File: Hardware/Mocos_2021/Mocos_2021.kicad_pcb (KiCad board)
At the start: 2 copper layers, 124.5 x 86.1 mm, 90 parts, among them J1 USB_B_Mini, J2 SERIAL PORT, J3 Programming, Q1 IRFZ44ESTRLPBF, Q2 IRFZ44ESTRLPBF, Q3 IRFZ44ESTRLPBF, Q4 IRFZ44ESTRLPBF, Q5 IRFZ44ESTRLPBF, Q6 IRFZ44ESTRLPBF, U1 DRV8302, U2 STM32F40X_LQFP64, U3 3.3V OKI, X1 8MHz, 10ppm

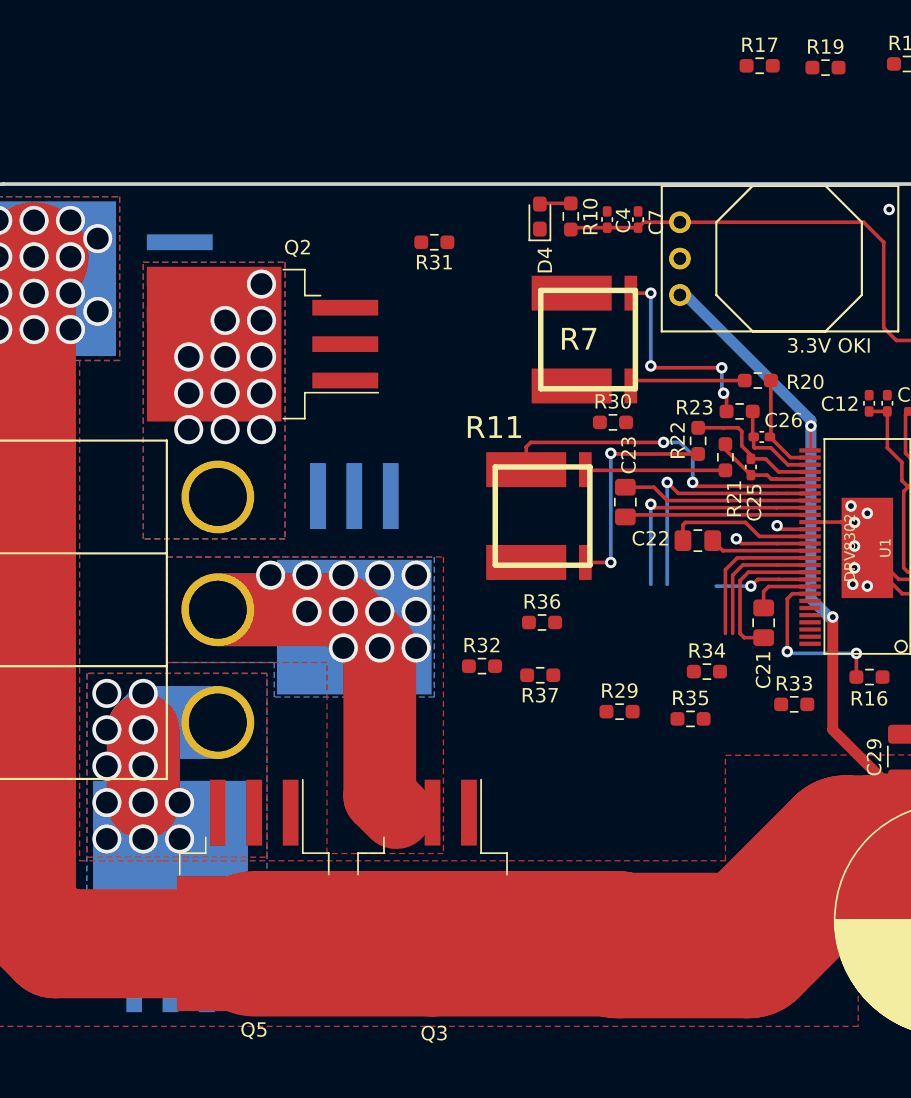
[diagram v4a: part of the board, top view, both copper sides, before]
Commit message: Finished routing all but the sense resistors
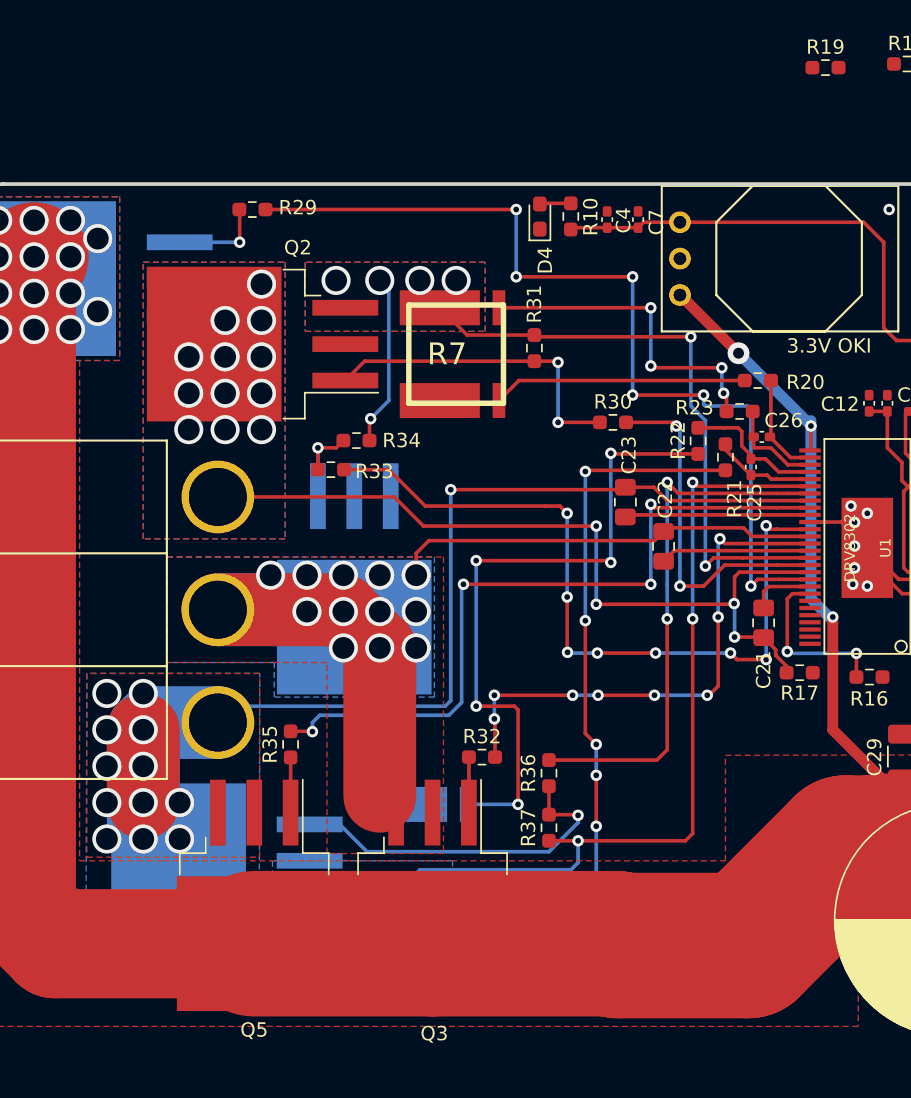
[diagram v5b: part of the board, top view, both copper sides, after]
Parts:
- R11: moved to B.Cu
- moved R29 43.4 mm to (85.1, 71.0)
- moved R17 42.5 mm to (123.3, 103.3), turned to 180 degrees
- moved R33 36.3 mm to (90.6, 89.2)
- moved R34 29.3 mm to (92.4, 87.1), turned to 180 degrees
- moved R35 28.0 mm to (87.8, 108.3), turned to 90 degrees
- moved R11 24.8 mm to (98.9, 115.8), turned to 90 degrees
- moved R37 10.7 mm to (105.8, 114.1), turned to 90 degrees
- moved R36 10.5 mm to (105.8, 110.3), turned to 90 degrees
- moved R31 10.2 mm to (104.8, 80.7), turned to 270 degrees
- moved R7 9.26 mm to (101.2, 81.1)
- moved R32 6.35 mm to (101.1, 109.2)
- moved Q6 4.66 mm to (83.3, 116.5), turned to 180 degrees
- moved C22 2.43 mm to (113.8, 94.5), turned to 270 degrees
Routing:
- net M_H1: track 6.74 -> 64.3 mm, vias 1 -> 6
- net M_L2: track 2.57 -> 53.1 mm, vias 1 -> 8
- net H1_VS: track 10.6 -> 56.9 mm, vias 12 -> 16
- net H3_VS: track 32.4 -> 76.3 mm, vias 12 -> 13
- net H1_LOW: track 10.7 -> 54.3 mm, vias 0 -> 7
- net Net-(R11-Pad3): track 9.80 -> 48.6 mm, vias 0 -> 5
- net M_H3: track 16.8 -> 51.4 mm, vias 1 -> 4
- net H3_LOW: track 23.9 -> 58.1 mm, vias 2 -> 3
- net M_H2: track 5.28 -> 37.0 mm, vias 1 -> 8
- net Net-(R11-Pad4): track 15.5 -> 46.7 mm, vias 2 -> 5
- net Net-(Q6-Pad2): track 0.00 -> 24.9 mm, vias 0 -> 1
- net Net-(Q2-Pad2): track 0.00 -> 22.6 mm, vias 0 -> 2
- net M_L3: track 17.4 -> 37.5 mm, vias 1 -> 2
- net H2_VS: track 46.2 -> 64.1 mm
- net M_L1: track 9.76 -> 24.6 mm, vias 0 -> 2
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- added copper zone on B.Cu, net H1_LOW
- added copper zone on F.Cu, net H1_LOW
- added copper zone on B.Cu, net H3_LOW

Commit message: Finished layout and generated Gerbs
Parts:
- added G***: LOGO, Anthony's Silkscreens:W, B.Cu at (162.4, 149.2)
- added G***: LOGO, MRDT_Silkscreens:z_sig_Anthony_Robles_15mmx8.2mm, F.Cu at (162.3, 149.4)
- U1: value DRV8302 -> DRV8302DCA
- U2: value STM32F40X_LQFP64 -> STM32F405RGT6
- moved R18 46.1 mm to (119.8, 105.6), turned to 90 degrees
- moved R19 20.3 mm to (127.7, 81.2), turned to 180 degrees
- moved C38 5.04 mm to (173.8, 95.8)
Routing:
- net SENSE2: track 9.45 -> 66.9 mm, vias 0 -> 4
- net SENSE3: track 12.3 -> 65.6 mm, vias 0 -> 4
- net SENSE1: track 6.44 -> 41.0 mm, vias 0 -> 4
- net H3_VS: track 76.3 -> 89.0 mm, vias 13 -> 15
- net H2_VS: track 64.1 -> 76.0 mm, vias 12 -> 14
- net Net-(C38-Pad1): track 23.8 -> 26.4 mm, vias 2 -> 4
- net Net-(J3-Pad2): track 56.2 -> 58.2 mm
- net H2_LOW: track 35.9 -> 34.1 mm, vias 30 -> 225
- net +3V3: track 164.0 -> 165.1 mm
- net H1_VS: vias 16 -> 14
- net BR_SO1: vias 4 -> 2
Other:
- board text added: "Drive Brushless Motor Controllers, Rev1 Based on Vesc 4.12 Mars Rover Design Team Missouri S&T, 2022 Anthony Robles"
- board text added: "KEEP OUT ZONE"

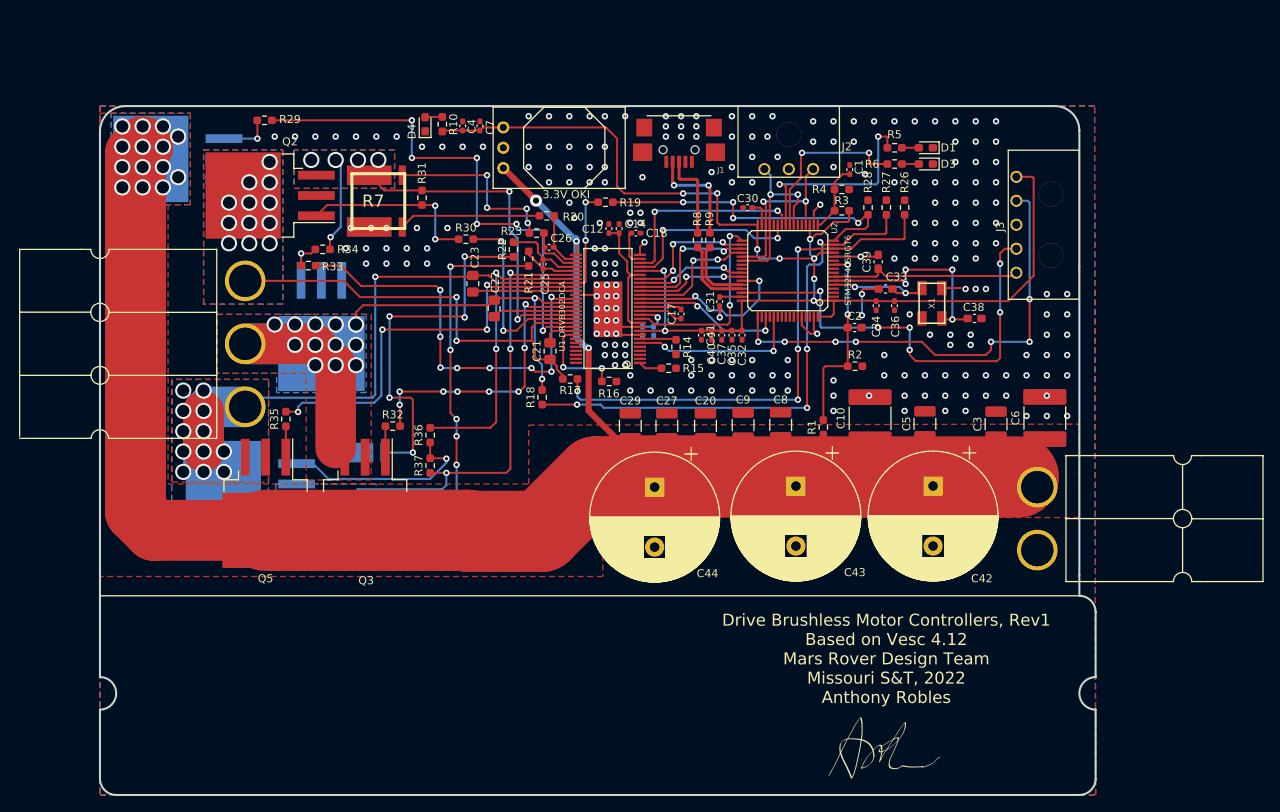
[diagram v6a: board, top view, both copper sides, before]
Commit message: Finished BOM and Fixed some Layout errors such as trace tolerance
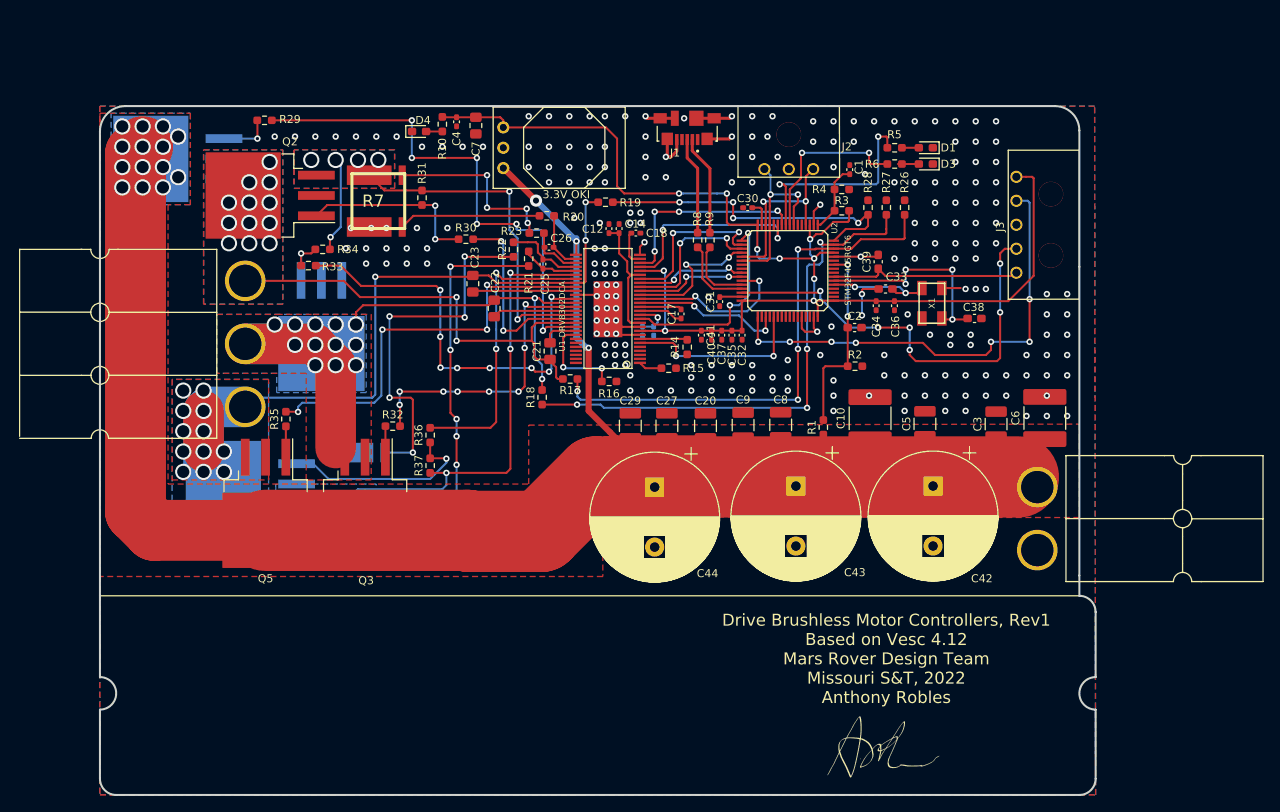
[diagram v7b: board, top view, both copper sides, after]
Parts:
- C7: footprint Capacitor_SMD:C_0402_1005Metric_Pad0.74x0.62mm_HandSolder -> Capacitor_SMD:C_0805_2012Metric_Pad1.18x1.45mm_HandSolder
- J1: value USB_B_Mini -> USB_B_Micro; footprint crf1:USB-UX60R-MB-5ST -> MRDT_Connectors:MOLEX_47346-0001
- moved G*** 8.01 mm to (162.2, 141.2)
- moved J1 4.07 mm to (137.9, 70.7)
- moved R14 1.40 mm to (137.9, 99.3)
- moved D4 1.17 mm to (104.4, 72.4), turned to 0 degrees
- moved C4 0.92 mm to (109.1, 71.2), turned to 270 degrees
- moved C7 0.51 mm to (111.5, 71.6), turned to 270 degrees
- moved G*** 0.18 mm to (162.2, 149.2)
- turned R10 to 270 degrees
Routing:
- net H2_LOW: track 34.1 -> 49.5 mm, vias 225 -> 223
- net L3: track 16.7 -> 20.5 mm, vias 3 -> 2
- net Net-(J3-Pad4): track 56.2 -> 54.1 mm
- net L2: track 17.3 -> 19.0 mm
- net DC_CAL: track 24.2 -> 25.8 mm
- net FAULT: track 21.4 -> 23.1 mm
- net BR_SO1: track 23.3 -> 24.9 mm
- net Net-(R14-Pad1): track 4.72 -> 5.95 mm
- net Net-(J1-Pad3): track 11.0 -> 12.2 mm
- net L1: track 16.7 -> 17.6 mm
- net +3V3: track 165.1 -> 164.2 mm
- net Net-(J1-Pad2): track 13.3 -> 12.6 mm, vias 2 -> 0
- net BR_SO2: vias 2 -> 4
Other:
- net class Default: clearance 0.2 -> 0.127; trace_width 0.25 -> 0.254
- net class Power added: clearance 0.127, trace_width 0.254, via_dia 0.8, via_drill 0.4
- net class Signal added: clearance 0.127, trace_width 0.254, via_dia 0.8, via_drill 0.4
- rule trace_clearance: 0.2 -> 0.127
- rule trace_min: 0.2 -> 0.254
